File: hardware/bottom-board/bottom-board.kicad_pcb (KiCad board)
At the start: 4 copper layers, 39 x 110 mm, 51 parts, among them J1 01x10 Female Pin Header, J2 PWR, J3 01x10 Female Pin Header, Q1 2N3904, Q2 2N3906, Q3 2N3904, Q4 2N3906, U1 TL084, U2 NE5517

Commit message: feature: docs
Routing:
- net +12V: track 28.3 -> 29.1 mm
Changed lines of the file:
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@@
 		(sheetname "/")
 		(sheetfile "bottom-board.kicad_sch")
+		(clearance 0.15)
 		(attr smd)
 		(fp_line
@@
 	)
 	(via
-		(at 40.5 57.75)
+		(at 41.3 57.75)
 		(size 0.8)
 		(drill 0.4)
@@
 	)
 	(segment
+		(start 41.3 57.75)
+		(end 39.38 57.75)
+		(width 0.89)
+		(layer "In2.Cu")
+		(net 6)
+	)
+	(segment
 		(start 23.601079 50.461079)
 		(end 23.601079 54.601079)
@@
 	)
 	(segment
-		(start 40.5 57.75)
-		(end 39.38 57.75)
-		(width 0.89)
-		(layer "In2.Cu")
-		(net 6)
-	)
-	(segment
 		(start 56.401079 116.461079)
 		(end 50.876 110.936)
@@
 	)
 	(segment
-		(start 37.3125 53.25)
-		(end 37.3125 53.525)
+		(start 42.3 36.1)
+		(end 42.3 53.32)
 		(width 0.25)
 		(layer "F.Cu")
@@
 	)
 	(segment
-		(start 42.3 36.1)
-		(end 42.3 53.32)
+		(start 40 55.62)
+		(end 39.56 56.06)
 		(width 0.25)
 		(layer "F.Cu")
@@
 	)
 	(segment
-		(start 40 55.62)
-		(end 39.56 56.06)
+		(start 37.3125 53.25)
+		(end 37.3125 53.525)
 		(width 0.25)
 		(layer "F.Cu")
@@
 	)
 	(segment
-		(start 40 55.62)
-		(end 37.905 53.525)
+		(start 37.905 53.525)
+		(end 40 55.62)
 		(width 0.25)
 		(layer "B.Cu")
@@
 	)
 	(segment
-		(start 37.905 53.525)
-		(end 37.3125 53.525)
+		(start 37.3125 53.525)
+		(end 37.905 53.525)
 		(width 0.25)
 		(layer "B.Cu")

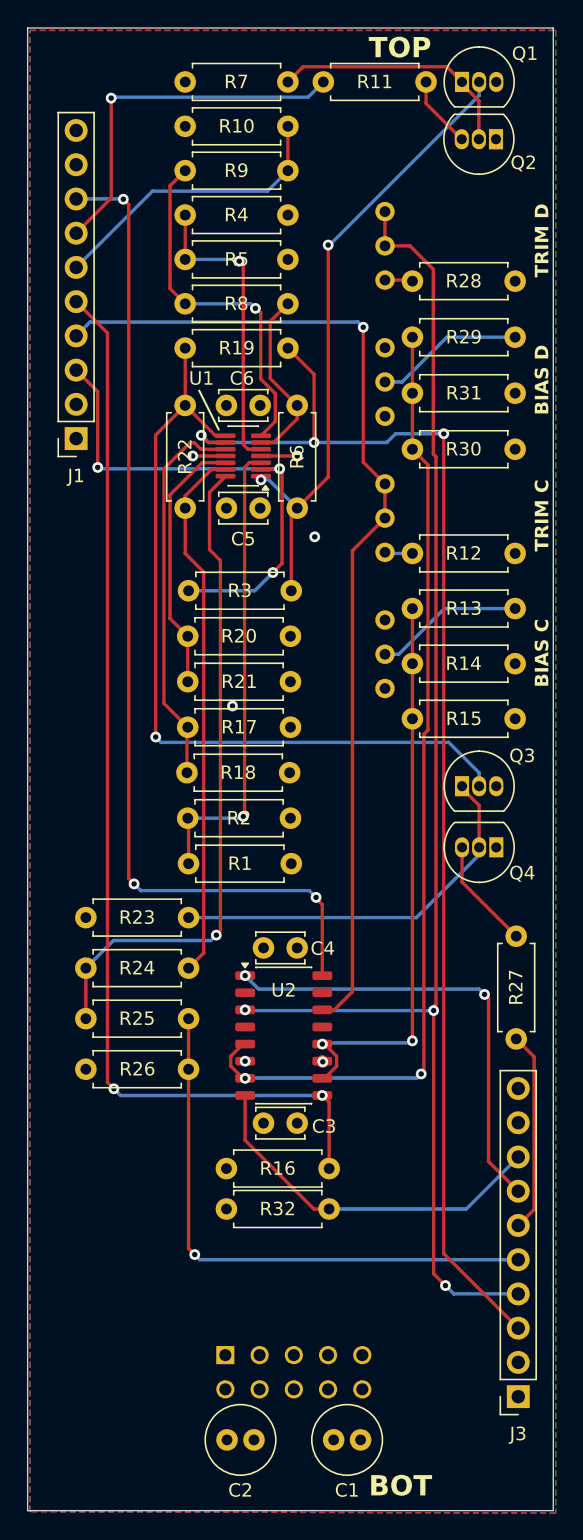
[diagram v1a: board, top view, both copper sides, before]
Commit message: feature: optional DIP footprint on PCB for TL0X4 op amps
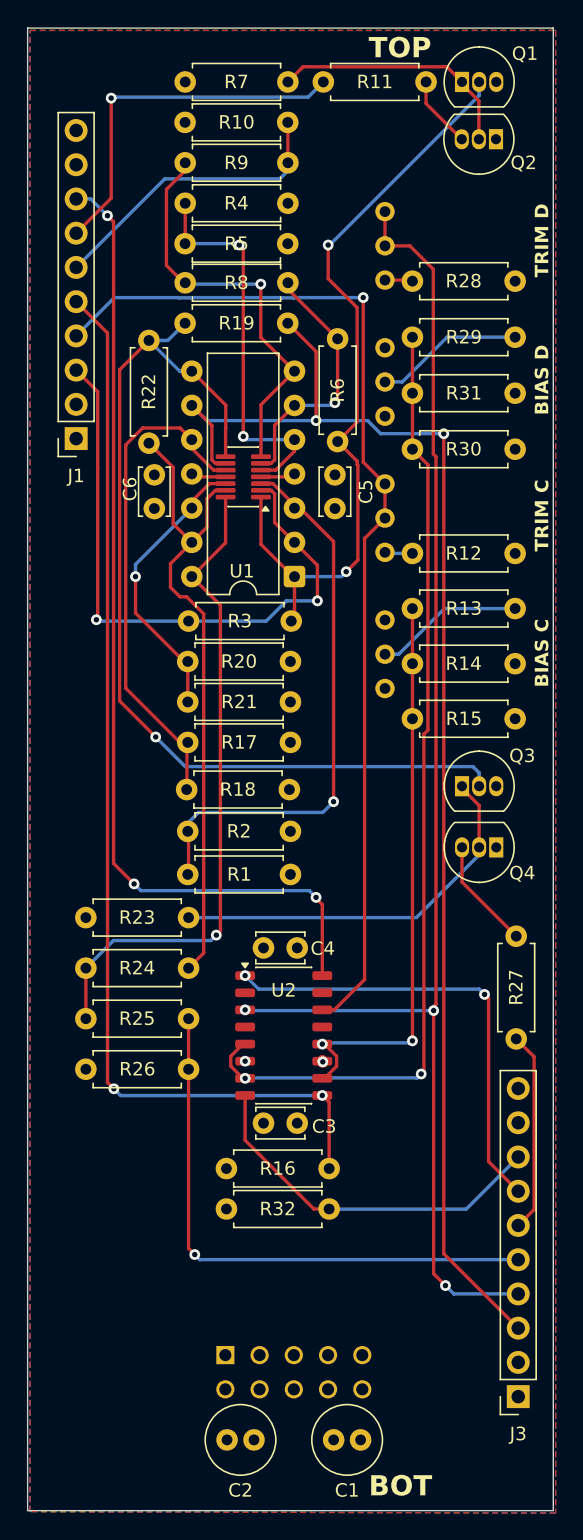
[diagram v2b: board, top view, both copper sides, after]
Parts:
- added U1: TL084, Package_DIP:DIP-14_W7.62mm, F.Cu at (39.8, 60.7)
- moved C6 11.0 mm to (29.4, 55.6), turned to 90 degrees
- moved C5 6.07 mm to (42.8, 53.1), turned to -90 degrees
- moved R6 5.78 mm to (43.0, 50.7)
- moved R22 5.52 mm to (29.0, 43.2)
- moved R3 2.25 mm to (31.9, 64.0)
- moved R20 1.88 mm to (31.9, 67.0)
- moved R19 1.85 mm to (39.3, 41.9)
- moved R8 1.56 mm to (31.7, 38.9)
- moved U1 1.55 mm to (36.0, 53.3)
- moved R21 1.50 mm to (39.5, 70.0)
- moved R18 1.25 mm to (31.8, 76.5)
- moved R5 1.17 mm to (39.3, 36.0)
- moved R17 1.12 mm to (39.5, 73.0)
- moved R2 0.97 mm to (31.9, 79.6)
- moved R4 0.88 mm to (31.7, 33.0)
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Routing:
- net Net-(Q3-B): track 59.8 -> 72.3 mm
- net Net-(Q1-B): track 47.7 -> 58.0 mm
- net /OFFSET_C: track 37.7 -> 46.7 mm, vias 3 -> 2
- net Net-(U1C-+): track 28.9 -> 37.5 mm
- net Net-(U1D--): track 39.9 -> 48.0 mm
- net Net-(U1A-+): track 34.9 -> 41.9 mm
- net Net-(U1B-+): track 22.5 -> 29.2 mm, vias 1 -> 2
- net Net-(U1B--): track 13.3 -> 19.4 mm, vias 0 -> 1
- net /OFFSET_D: track 97.0 -> 102.1 mm, vias 3 -> 2
- net Net-(R8-Pad1): track 26.7 -> 30.6 mm
- net /IN_C: track 75.6 -> 78.5 mm
- net Net-(U1D-+): track 19.5 -> 21.4 mm, vias 0 -> 1
- net /COMMON_C: track 74.6 -> 73.2 mm
- net -12V: track 50.8 -> 51.9 mm, vias 3 -> 1
- net +12V: track 29.1 -> 28.0 mm, vias 3 -> 1

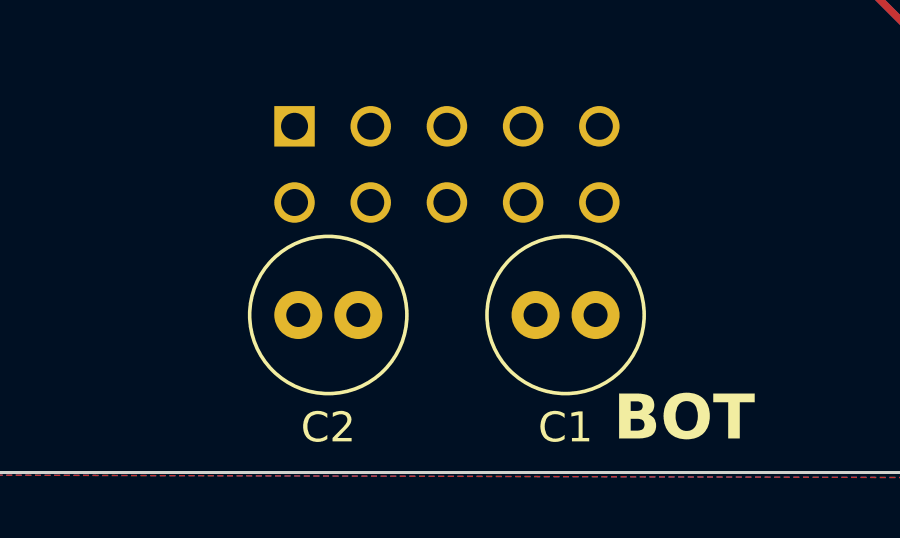
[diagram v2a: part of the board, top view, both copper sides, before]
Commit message: fix: inverted power pins on op amps
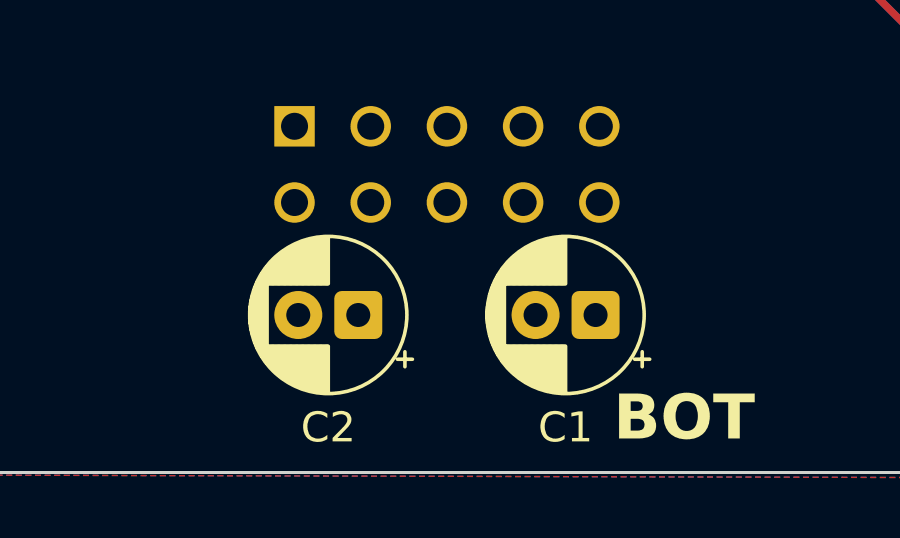
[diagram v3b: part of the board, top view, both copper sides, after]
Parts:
- C1, C2: footprint Eurorack Common:C_Radial_D5.0mm_H11.0mm_P2.00mm -> Eurorack Common:CP_Radial_D5.0mm_H11.0mm_P2.00mm
